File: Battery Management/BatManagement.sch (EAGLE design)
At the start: 19 parts, among them J1 RASPBERRYPI-40-PIN-GPIO_PTH, SW1 100SP1T2B4M6QE, X1 87758-1416, X2 87758-1416, X3 22-23-2031, X4 22-23-2031

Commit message: Added jumper for 6V motors
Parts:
- added J2: (no value), SparkFun-Connectors:CONN_02
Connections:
- net 5V: now also J2.2
- net ENC1A_1: now also J1.SDA
- net ENC1A_2: now also J1.SCLK
- net ENC1B_1: now also J1.SCL
- net ENC1B_2: now also J1.MISO
- net ENC2A_1: now also J1.TXO
- net ENC2A_2: now also J1.MOSI
- net ENC2B_1: now also J1.RXI
- net ENC2B_2: now also J1.CE0
- net IN3_1: no longer X2-12.S
- net IN3_2: now also X2-12.S
- net VMOT: now also J2.1
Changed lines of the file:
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@@
 </variantdefs>
 <classes>
-<class number="0" name="default" width="0.3" drill="0.25">
+<class number="0" name="default" width="0.4" drill="0.25">
 <clearance class="0" value="0.15"/>
 </class>
-<class number="1" name="Power" width="0.7" drill="0.25">
+<class number="1" name="Power" width="1" drill="0.25">
 <clearance class="1" value="0.15"/>
 </class>
@@
 <part name="SUPPLY13" library="supply2" library_urn="urn:adsk.eagle:library:372" deviceset="GND" device=""/>
 <part name="3_3VREG" library="linear" library_urn="urn:adsk.eagle:library:262" deviceset="78*" device="T" package3d_urn="urn:adsk.eagle:package:16414/1" technology="05"/>
+<part name="J2" library="SparkFun-Connectors" library_urn="urn:adsk.eagle:library:513" deviceset="CONN_02" device="" package3d_urn="urn:adsk.eagle:package:38039/1"/>
 </parts>
 <sheets>
@@
 <attribute name="NAME" x="20.32" y="-6.985" size="1.778" layer="95"/>
 <attribute name="VALUE" x="20.32" y="-9.525" size="1.778" layer="96"/>
+</instance>
+<instance part="J2" gate="G$1" x="182.88" y="-12.7" smashed="yes">
+<attribute name="VALUE" x="180.34" y="-17.526" size="1.778" layer="96" font="vector"/>
+<attribute name="NAME" x="180.34" y="-7.112" size="1.778" layer="95" font="vector"/>
 </instance>
 </instances>
@@
 <label x="236.22" y="99.06" size="1.778" layer="95"/>
 </segment>
+<segment>
+<pinref part="J2" gate="G$1" pin="1"/>
+<wire x1="190.5" y1="-12.7" x2="203.2" y2="-12.7" width="0.1524" layer="91"/>
+<label x="203.2" y="-12.7" size="1.778" layer="95"/>
+</segment>
 </net>
 <net name="LED1" class="0">
@@
 </segment>
 <segment>
-<pinref part="X2" gate="-12" pin="S"/>
-<wire x1="213.36" y1="86.36" x2="236.22" y2="86.36" width="0.1524" layer="91"/>
-<label x="236.22" y="86.36" size="1.778" layer="95"/>
-</segment>
-<segment>
 <pinref part="J1" gate="G$1" pin="GP18#"/>
 <wire x1="48.26" y1="93.98" x2="55.88" y2="93.98" width="0.1524" layer="91"/>
@@
 <label x="172.72" y="121.92" size="1.778" layer="95"/>
 </segment>
+<segment>
+<pinref part="J1" gate="G$1" pin="SDA"/>
+<wire x1="48.26" y1="129.54" x2="55.88" y2="129.54" width="0.1524" layer="91"/>
+<label x="55.88" y="129.54" size="1.778" layer="95"/>
+</segment>
 </net>
 <net name="ENC1B_1" class="0">
@@
 <label x="172.72" y="119.38" size="1.778" layer="95"/>
 </segment>
+<segment>
+<pinref part="J1" gate="G$1" pin="SCL"/>
+<wire x1="48.26" y1="127" x2="55.88" y2="127" width="0.1524" layer="91"/>
+<label x="55.88" y="127" size="1.778" layer="95"/>
+</segment>
 </net>
 <net name="5V" class="1">
@@
 <label x="185.42" y="30.48" size="1.778" layer="95"/>
 </segment>
+<segment>
+<pinref part="J2" gate="G$1" pin="2"/>
+<wire x1="190.5" y1="-10.16" x2="203.2" y2="-10.16" width="0.1524" layer="91"/>
+<label x="203.2" y="-10.16" size="1.778" layer="95"/>
+</segment>
 </net>
 <net name="ENC2A_1" class="0">
@@
 <label x="233.68" y="127" size="1.778" layer="95"/>
 </segment>
+<segment>
+<pinref part="J1" gate="G$1" pin="TXO"/>
+<wire x1="48.26" y1="121.92" x2="55.88" y2="121.92" width="0.1524" layer="91"/>
+<label x="55.88" y="121.92" size="1.778" layer="95"/>
+</segment>
 </net>
 <net name="ENC2B_1" class="0">
@@
 <label x="233.68" y="129.54" size="1.778" layer="95"/>
 </segment>
+<segment>
+<pinref part="J1" gate="G$1" pin="RXI"/>
+<wire x1="48.26" y1="119.38" x2="55.88" y2="119.38" width="0.1524" layer="91"/>
+<label x="55.88" y="119.38" size="1.778" layer="95"/>
+</segment>
 </net>
 <net name="IN1_2" class="0">
@@
 <label x="175.26" y="88.9" size="1.778" layer="95"/>
 </segment>
+<segment>
+<pinref part="J1" gate="G$1" pin="SCLK"/>
+<wire x1="48.26" y1="114.3" x2="55.88" y2="114.3" width="0.1524" layer="91"/>
+<label x="55.88" y="114.3" size="1.778" layer="95"/>
+</segment>
 </net>
 <net name="ENC1B_2" class="0">
@@
 <label x="175.26" y="86.36" size="1.778" layer="95"/>
 </segment>
+<segment>
+<pinref part="J1" gate="G$1" pin="MISO"/>
+<wire x1="48.26" y1="111.76" x2="55.88" y2="111.76" width="0.1524" layer="91"/>
+<label x="55.88" y="111.76" size="1.778" layer="95"/>
+</segment>
 </net>
 <net name="ENC2B_2" class="0">
@@
 <label x="236.22" y="96.52" size="1.778" layer="95"/>
 </segment>
+<segment>
+<pinref part="J1" gate="G$1" pin="CE0"/>
+<wire x1="48.26" y1="106.68" x2="55.88" y2="106.68" width="0.1524" layer="91"/>
+<label x="55.88" y="106.68" size="1.778" layer="95"/>
+</segment>
 </net>
 <net name="ENC2A_2" class="0">
@@
 <wire x1="213.36" y1="93.98" x2="236.22" y2="93.98" width="0.1524" layer="91"/>
 <label x="236.22" y="93.98" size="1.778" layer="95"/>
+</segment>
+<segment>
+<pinref part="J1" gate="G$1" pin="MOSI"/>
+<wire x1="48.26" y1="109.22" x2="55.88" y2="109.22" width="0.1524" layer="91"/>
+<label x="55.88" y="109.22" size="1.778" layer="95"/>
 </segment>
 </net>
@@
 <wire x1="15.24" y1="124.46" x2="17.78" y2="124.46" width="0.1524" layer="91"/>
 <wire x1="17.78" y1="124.46" x2="17.78" y2="121.92" width="0.1524" layer="91"/>
+<junction x="17.78" y="124.46"/>
 </segment>
 <segment>
@@
 <wire x1="48.26" y1="86.36" x2="55.88" y2="86.36" width="0.1524" layer="91"/>
 <label x="55.88" y="86.36" size="1.778" layer="95"/>
+</segment>
+<segment>
+<pinref part="X2" gate="-12" pin="S"/>
+<wire x1="213.36" y1="86.36" x2="236.22" y2="86.36" width="0.1524" layer="91"/>
+<label x="236.22" y="86.36" size="1.778" layer="95"/>
 </segment>
 </net>
@@
 </sheet>
 </sheets>
+<errors>
+</errors>
 </schematic>
 </drawing>

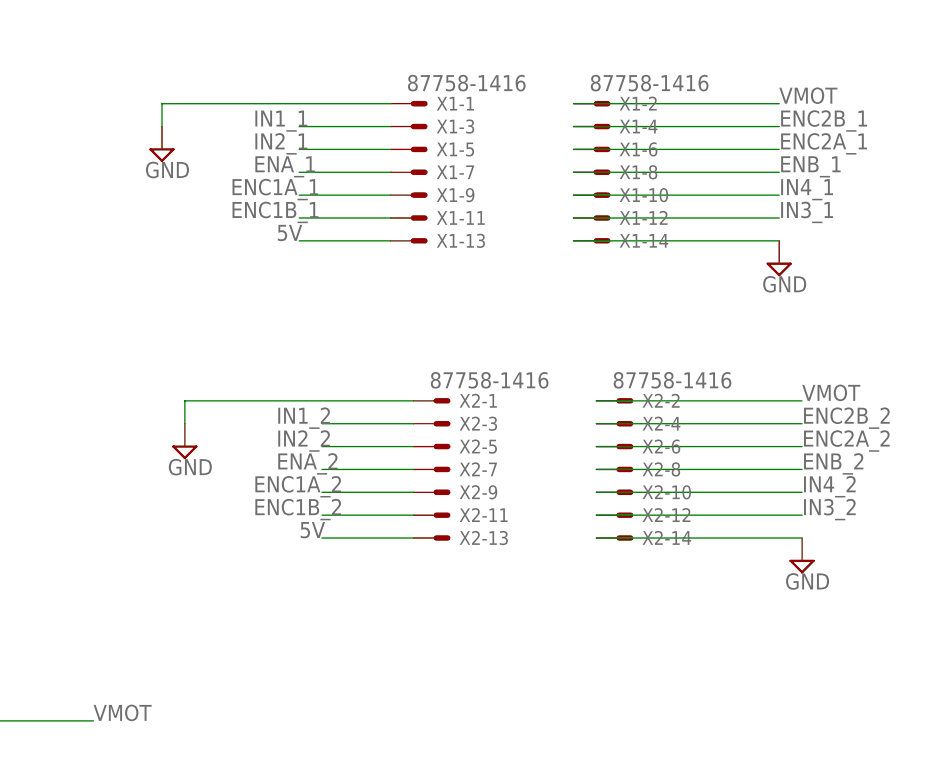
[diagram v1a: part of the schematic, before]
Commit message: Changed to standard header for mdriver connection
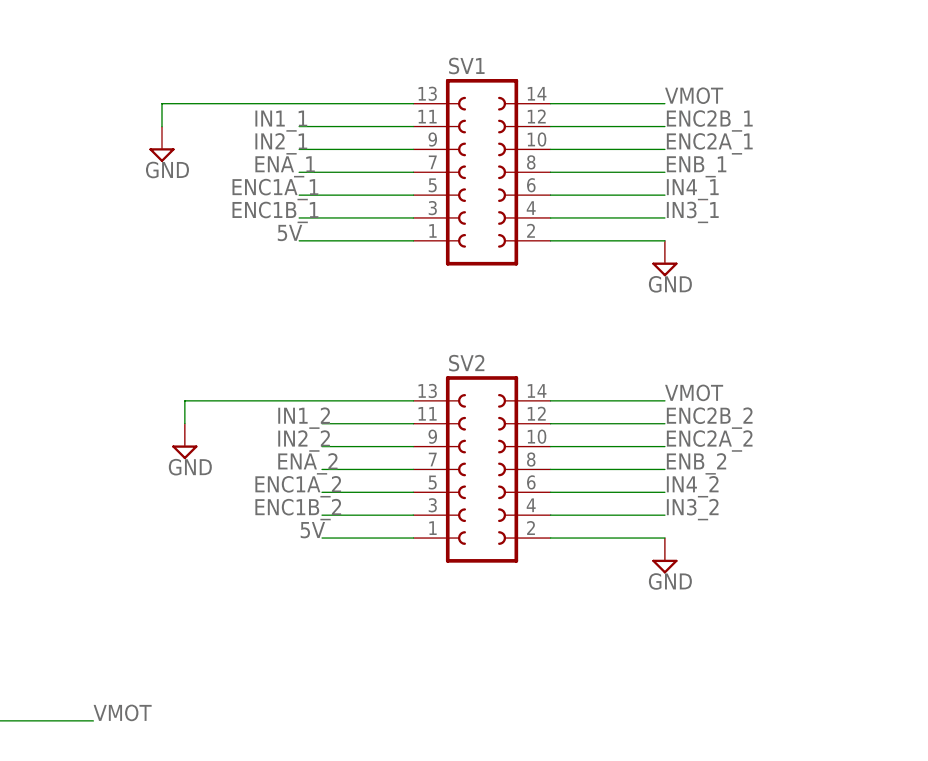
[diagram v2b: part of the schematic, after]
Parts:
- removed X1, X2: 87758-1416, con-molex:87758-1416
- added SV1, SV2: (no value), con-lsta:FE07-2
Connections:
- net 5V: now also SV1.1, SV2.1; no longer X1-13.S, X2-13.S
- net ENA_1: now also SV1.7; no longer X1-7.S
- net ENA_2: now also SV2.7; no longer X2-7.S
- net ENB_1: now also SV1.8; no longer X1-8.S
- net ENB_2: now also SV2.8; no longer X2-8.S
- net ENC1A_1: now also SV1.5; no longer X1-9.S
- net ENC1A_2: now also SV2.5; no longer X2-9.S
- net ENC1B_1: now also SV1.3; no longer X1-11.S
- net ENC1B_2: now also SV2.3; no longer X2-11.S
- net ENC2A_1: now also SV1.10; no longer X1-6.S
- net ENC2A_2: now also SV2.10; no longer X2-6.S
- net ENC2B_1: now also SV1.12; no longer X1-4.S
- net ENC2B_2: now also SV2.12; no longer X2-4.S
- net GND: now also SV1.13, SV1.2, SV2.13, SV2.2; no longer X1-1.S, X1-14.S, X2-1.S, X2-14.S
- net IN1_1: now also SV1.11; no longer X1-3.S
- net IN1_2: now also SV2.11; no longer X2-3.S
- net IN2_1: now also SV1.9; no longer X1-5.S
- net IN2_2: now also SV2.9; no longer X2-5.S
- net IN3_1: now also SV1.4; no longer X1-12.S
- net IN3_2: now also SV2.4; no longer X2-12.S
- net IN4_1: now also SV1.6; no longer X1-10.S
- net IN4_2: now also SV2.6; no longer X2-10.S
- net VMOT: now also SV1.14, SV2.14; no longer X1-2.S, X2-2.S
